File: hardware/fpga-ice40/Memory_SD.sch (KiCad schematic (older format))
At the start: 6 parts, among them J2 MicroSD_Molex_1040310811

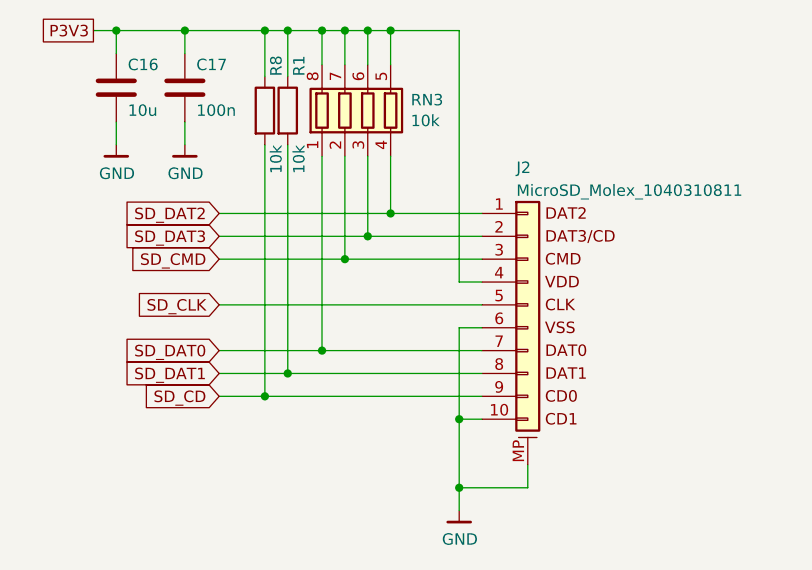
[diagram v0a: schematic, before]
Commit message: Finished routing all nets, including power distribution
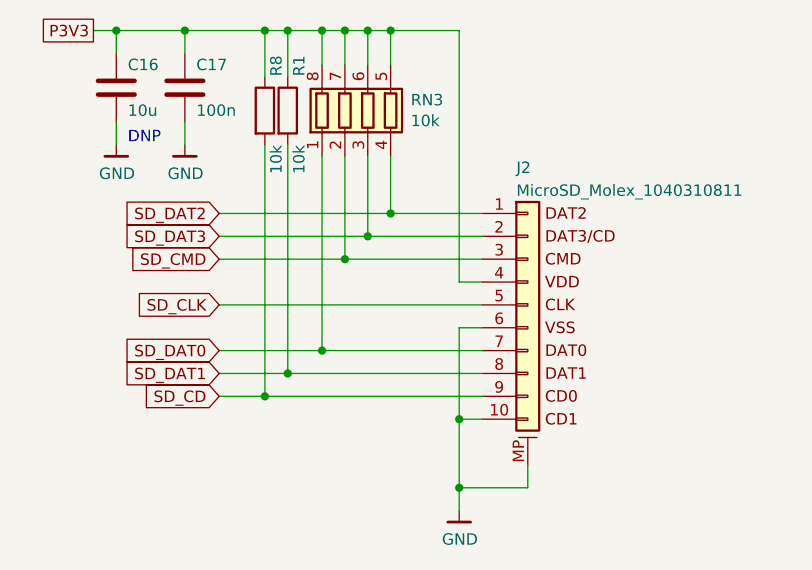
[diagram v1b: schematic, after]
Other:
- note added: "DNP"
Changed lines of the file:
@@
 Wire Wire Line
 	5700 4100 6100 4100
+Text Notes 4550 3800 0    50   ~ 0
+DNP
 $EndSCHEMATC
